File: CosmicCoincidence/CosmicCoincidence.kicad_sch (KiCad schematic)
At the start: 29 parts, among them J1 SJ-43515RS-SMT-TR, J10 Micro_SD_Card, J11 OLED Header, J2 SJ-43515RS-SMT-TR, J3 SJ-43515RS-SMT-TR, J4 SJ-43515RS-SMT-TR, J5 SJ-43515RS-SMT-TR, J6 SJ-43515RS-SMT-TR, J7 SJ-43515RS-SMT-TR, J8 SJ-43515RS-SMT-TR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

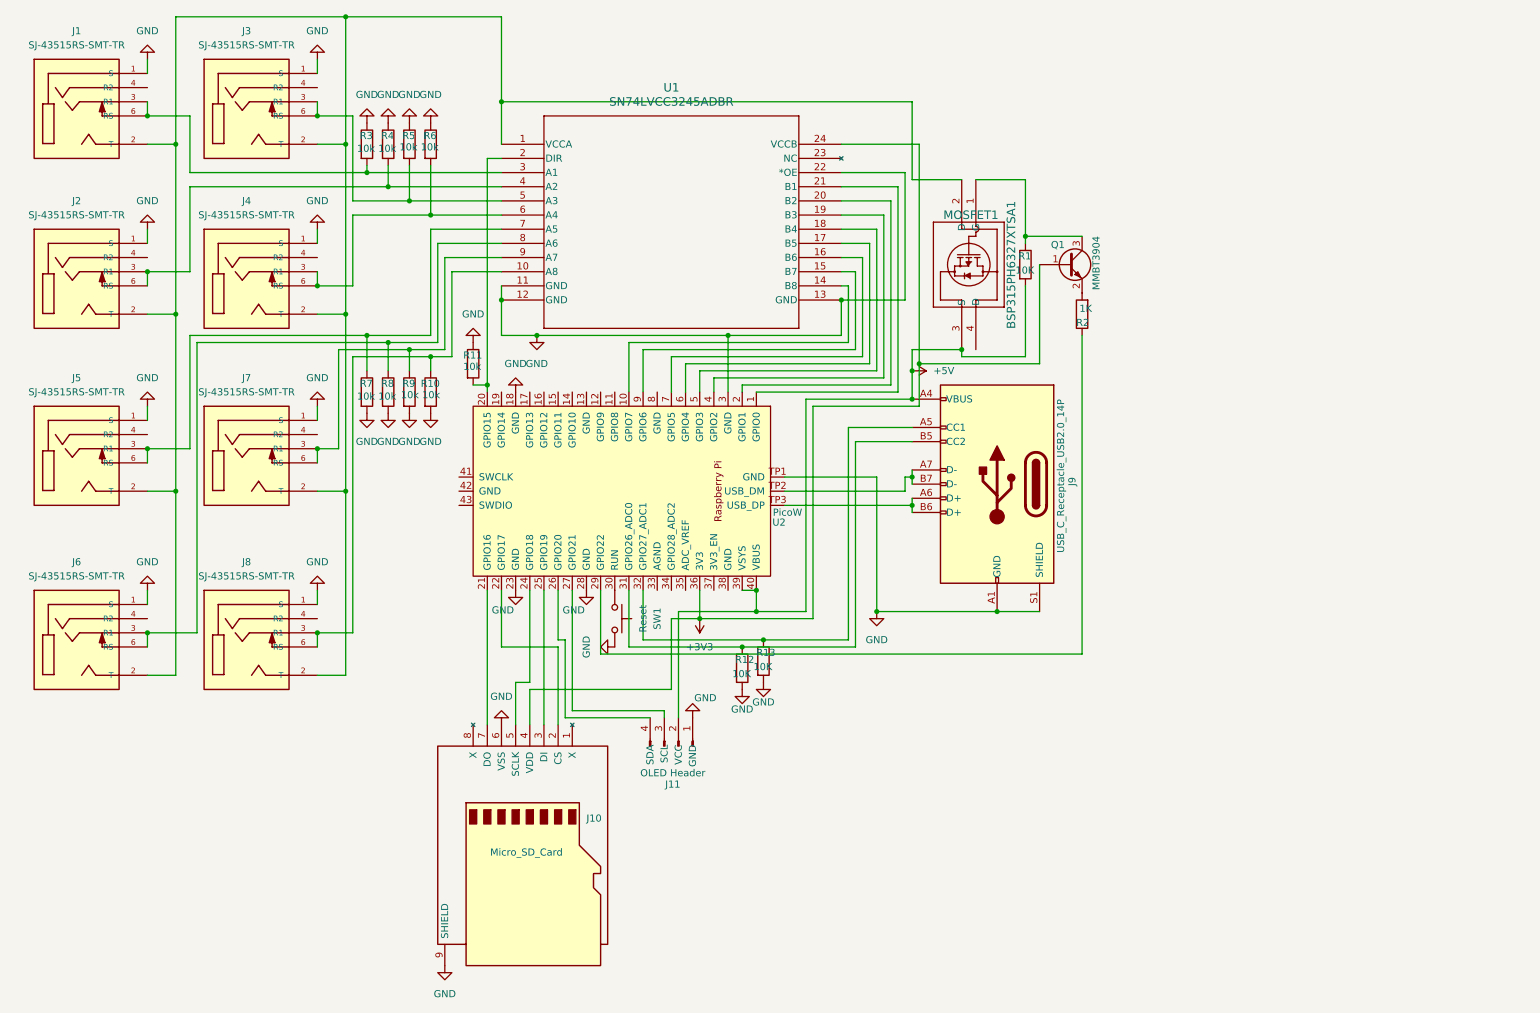
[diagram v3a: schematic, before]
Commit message: clean up schematic; add spice test schematic; change power switching circuit
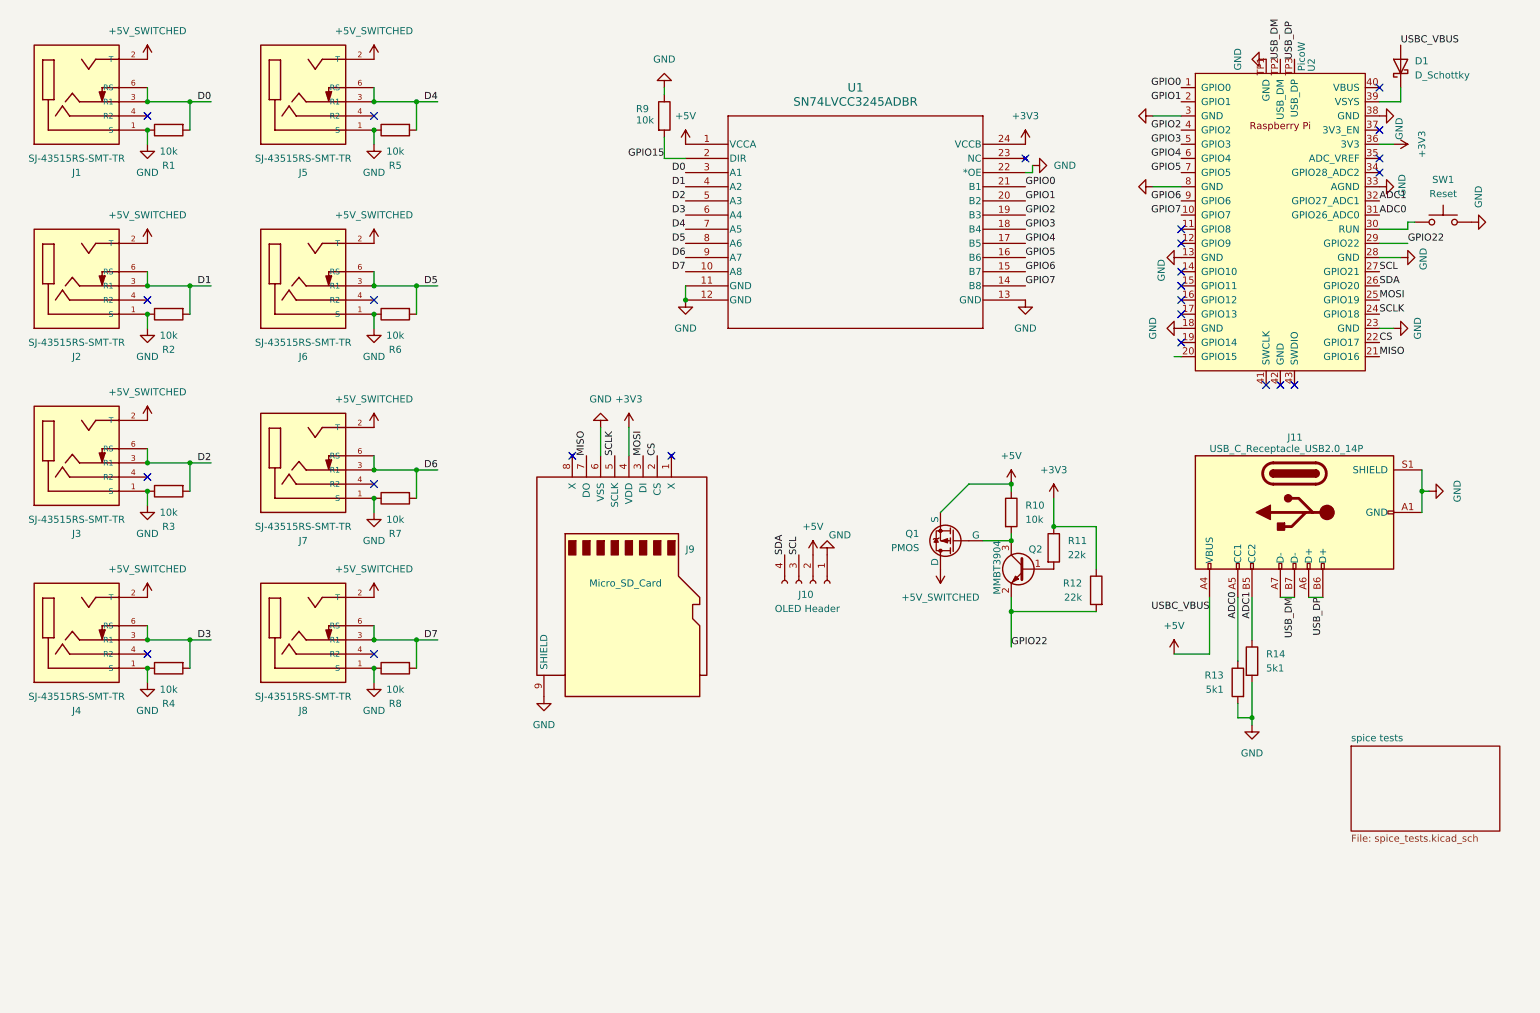
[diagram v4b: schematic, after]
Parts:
- removed MOSFET1: BSP315PH6327XTSA1, BSP315PH6327XTSA1:PG-SOT223-4_INF, symbol BSP315PH6327XTSA1:BSP315PH6327XTSA1
- removed R9: 10k, Resistor_SMD:R_0805_2012Metric, symbol Device:R
- added D1: D_Schottky, Diode_SMD:D_SOD-123, symbol Device:D_Schottky
- added Q1: PMOS, Package_TO_SOT_SMD:SOT-23, symbol Simulation_SPICE:PMOS
- added R11: 22k, Resistor_SMD:R_0805_2012Metric, symbol Device:R
- added R14: 5k1, Resistor_SMD:R_0805_2012Metric, symbol Device:R
- J10: renamed from J11; footprint Connector_PinHeader_2.54mm:PinHeader_1x04_P2.54mm_Vertical -> Connector_PinSocket_2.54mm:PinSocket_1x04_P2.54mm_Horizontal; symbol Connector:Conn_01x04_Pin -> Connector:Conn_01x04_Socket
- R1: value 10K -> 10k
- R12: value 10K -> 22k
- R13: value 10K -> 5k1
- R2: value 1K -> 10k
- SW1: footprint (none) -> Button_Switch_THT:SW_Tactile_SPST_Angled_PTS645Vx83-2LFS
- renumbered J9 to J11, J10 to J9, Q1 to Q2, R11 to R9
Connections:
- net +3V3: now also R12.1, R11.1; no longer Q2.1 (B)
- net +5V: now also R10.1, U1.1 (VCCA), D1.2 (A), Q1.3 (S); no longer R1.2, U2.39 (VSYS), U2.40 (VBUS)
- net GND: now also R1.1, R2.1, R7.1, R8.1, U2.13 (GND), U2.33 (AGND), U2.38 (GND), U2.8 (GND), R14.2; no longer R10.2, R12.2, R7.2, R8.2
- net D7: now reaches J8.3 (R1), J8.6 (RS), U1.10 (A8)
- net D7: now also R8.2; no longer R10.1
- net SCL: now reaches J10.3 (Pin_3), U2.27 (GPIO21)
- net SDA: now reaches J10.4 (Pin_4), U2.26 (GPIO20)
- net +5V_SWITCHED: now reaches J1.2 (T), J2.2 (T), J3.2 (T), J4.2 (T), J5.2 (T), J6.2 (T), J7.2 (T), J8.2 (T)
- net +5V_SWITCHED: now also Q1.1 (D); no longer U1.1 (VCCA)
- net D5: now reaches J6.3 (R1), J6.6 (RS), U1.8 (A6)
- net D5: now also R6.2; no longer R8.1
- net GPIO7: now reaches U1.14 (B8), U2.10 (GPIO7)
- net GPIO6: now reaches U1.15 (B7), U2.9 (GPIO6)
- net GPIO5: now reaches U1.16 (B6), U2.7 (GPIO5)
- net GPIO4: now reaches U1.17 (B5), U2.6 (GPIO4)
- net GPIO3: now reaches U1.18 (B4), U2.5 (GPIO3)
- net GPIO2: now reaches U1.19 (B3), U2.4 (GPIO2)
- net GPIO15: now reaches R9.2, U1.2 (DIR)
- net GPIO15: no longer U2.20 (GPIO15)
- net GPIO1: now reaches U1.20 (B2), U2.2 (GPIO1)
- net GPIO0: now reaches U1.21 (B1), U2.1 (GPIO0)
- net D0: now reaches J1.3 (R1), J1.6 (RS), U1.3 (A1)
- net D0: now also R1.2; no longer R3.2
- net D1: now reaches J2.3 (R1), J2.6 (RS), U1.4 (A2)
- net D1: now also R2.2; no longer R4.2
- net D2: now reaches J3.3 (R1), J3.6 (RS), U1.5 (A3)
- net D2: now also R3.2; no longer R5.2
- net D3: now reaches J4.3 (R1), J4.6 (RS), U1.6 (A4)
- net D3: now also R4.2; no longer R6.2
- net D4: now reaches J5.3 (R1), J5.6 (RS), U1.7 (A5)
- net D4: now also R5.2; no longer R7.1
- net D6: now reaches J7.3 (R1), J7.6 (RS), U1.9 (A7)
- net D6: now also R7.2
- net at Q2.3 (C): now also R10.2, Q1.2 (G); no longer R1.1
- net GPIO22: now reaches Q2.2 (E)
- net GPIO22: now also R12.2, U2.29 (GPIO22); no longer R2.2
- net CS: now reaches J9.2 (CS), U2.22 (GPIO17)
- net MOSI: now reaches J9.3 (DI), U2.25 (GPIO19)
- net SCLK: now reaches J9.5 (SCLK), U2.24 (GPIO18)
- net MISO: now reaches J9.7 (DO), U2.21 (GPIO16)
- net ADC0: now reaches J11.A5 (CC1), R13.1
- net ADC0: now also U2.31 (GPIO26_ADC0); no longer U2.32 (GPIO27_ADC1)
- net USB_DM: now reaches J11.A7 (D-), J11.B7 (D-), U2.TP2 (USB_DM)
- net USB_DP: now reaches J11.A6 (D+), J11.B6 (D+), U2.TP3 (USB_DP)
- new net: Q2.1 (B), R11.2
- new net: D1.1 (K), U2.39 (VSYS)
- new net ADC1: J11.B5 (CC2), R14.1, U2.32 (GPIO27_ADC1)
- no-connect marks 0 -> 25
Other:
- added sheet spice tests (spice_tests.kicad_sch)
- moved on the sheet: J1, J11, J9, Q2, R9, SW1, U1, U2
